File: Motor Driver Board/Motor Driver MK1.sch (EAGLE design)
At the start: 8 parts, among them X1 MAB8SH, X2 MAB8SH, X3 MAB8SH, X4 MAB8SH

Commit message: finished up schematic
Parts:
- removed U$1, U$2, U$4: DRV8825, CNC-Interface:DRV8825
- removed X2, X3, X4: MAB8SH, con-hirschmann:MAB8SH
- added AC1, XC1, YC1, ZC1: (no value), rcl:CPOL-USSANYO_SMD_F12
- added AC2, XC2, YC2, ZC2: (no value), rcl:C-USC0805
- added ADIR, AHOME, ASTP, EN, FAULT, XDIR, XHOME, XSTP, YDIR, YHOME, YSTP, ZDIR, ZHOME, ZSTP: PC817, optocoupler:PC817
- added ADIR_IN, AHOME_IN, ASTP_IN, FAULT_IN, RLED, XDIR_IN, XHOME_IN, XSTP_IN, YDIR_IN, YHOME_IN, YSTP_IN, ZDIR_IN, ZHOME_IN, ZSTP_IN: 330, resistor:R-US_R0805
- added ADIR_UP, AHOME_UP, EN_UP, FAULT_UP, XDIR_UP, XHOME_UP, YDIR_UP, YHOME_UP, ZDIR_UP, ZHOME_UP: 1k, resistor:R-US_R0805
- added ADRIVER, XDRIVER, YDRIVER: DRV8825, CNC-Interface:DRV8825
- added AFAULT, ASAMPLE, ESTOP, XFAULT, XSAMPLE, YFAULT, YSAMPLE, ZFAULT, ZSAMPLE: (no value), pinhead:PINHD-1X2
- added AHOME_OUT, FAULT_OUT, XHOME_OUT, YHOME_OUT, ZHOME_OUT: 100, resistor:R-US_R0805
- added AOUT, XOUT, YOUT, ZOUT: MAB8SH, con-hirschmann:MAB8SH
- added ASET, XSET, YSET, ZSET: (no value), pinhead:PINHD-2X3
- added ASTP_UP, EN_IN, XSTP_UP, YSTP_UP, ZSTP_UP: (no value), resistor:R-US_R0805
- added DB: PARALLEL PORT, con-thomas-betts:D-SUB25-H2R25ST
- added FAULTOUT: 4PIN, con-molex:22-23-2041
- added LED1: (no value), led:LEDCHIP-LED0805
- X1: value MAB8SH -> (none); device con-hirschmann:MAB8SH -> con-wago-500:W237-102
- renumbered U$3 to ZDRIVER
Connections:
- new net ASTP_UP: ADRIVER.STP, ASAMPLE.2, ASTP.COL, ASTP_UP.1
- new net DGND: ADIR.C, AHOME.EMIT, ASTP.C, DB-18.F, DB-19.F, DB-20.F, DB-21.F, DB-22.F, DB-23.F, DB-24.F, DB-25.F, EN.C, FAULT.EMIT, XDIR.C, XHOME.EMIT, XSTP.C, YDIR.C, YHOME.EMIT, YSTP.C, ZDIR.C, ZHOME.EMIT, ZSTP.C
- new net GND: AC1.-, AC2.2, ADIR.EMIT, ADRIVER.GND, AHOME.C, AOUT.3, AOUT.PE, ASTP.EMIT, EN.EMIT, ESTOP.2, FAULT.C, LED1.C, X1-2.KL, XC1.-, XC2.2, XDIR.EMIT, XDRIVER.GND, XHOME.C, XOUT.3, XOUT.PE, XSTP.EMIT, YC1.-, YC2.2, YDIR.EMIT, YDRIVER.GND, YHOME.C, YOUT.3, YOUT.PE, YSTP.EMIT, ZC1.-, ZC2.2, ZDIR.EMIT, ZDRIVER.GND, ZHOME.C, ZOUT.3, ZOUT.PE, ZSTP.EMIT
- new net N$15: ADRIVER.B1, AOUT.4
- new net N$16: ADRIVER.B2, AOUT.7
- new net N$17: LED1.A, RLED.1
- new net N$18: XDRIVER.STP, XSAMPLE.2, XSTP.COL, XSTP_UP.1
- new net N$19: XDRIVER.M2, XSET.2
- new net N$20: XDRIVER.M1, XSET.4
- new net N$21: XDRIVER.M0, XSET.6
- new net N$22: YDRIVER.M2, YSET.2
- new net N$23: YDRIVER.M1, YSET.4
- new net N$24: YDRIVER.M0, YSET.6
- new net N$25: ADRIVER.M2, ASET.2
- new net N$26: ADRIVER.M1, ASET.4
- new net N$27: ADRIVER.M0, ASET.6
- new net N$28: ZDRIVER.M2, ZSET.2
- new net N$29: ZDRIVER.M1, ZSET.4
- new net N$30: ZDRIVER.M0, ZSET.6
- new net N$33: ADRIVER.EN, EN.COL, EN_UP.1, ESTOP.1, XDRIVER.EN, YDRIVER.EN, ZDRIVER.EN
- new net N$35: EN.A, EN_IN.1
- new net N$37: AFAULT.2, FAULTOUT-3.S, ZDRIVER.FLT, ZFAULT.1
- new net N$38: XDIR.A, XDIR_IN.1
- new net N$39: XSTP.A, XSTP_IN.1
- new net N$40: YDIR.A, YDIR_IN.1
- new net N$41: YSTP.A, YSTP_IN.1
- new net N$42: DB-2.F, XDIR_IN.2
- new net N$43: DB-3.F, XSTP_IN.2
- new net N$44: DB-4.F, YDIR_IN.2
- new net N$45: DB-5.F, YSTP_IN.2
- new net N$46: ZSTP.A, ZSTP_IN.1
- new net N$47: ZDIR.A, ZDIR_IN.1
- new net N$48: DB-6.F, ZDIR_IN.2
- new net N$49: DB-7.F, ZSTP_IN.2
- new net N$50: ADIR.A, ADIR_IN.1
- new net N$51: ADIR_IN.2, DB-8.F
- new net N$52: ASTP_IN.2, DB-9.F
- new net N$53: ASTP.A, ASTP_IN.1
- new net N$54: DB-1.F, EN_IN.2
- new net N$55: DB-10.F, XHOME_OUT.2
- new net N$57: ADIR.COL, ADIR_UP.1, ADRIVER.DIR, ASAMPLE.1
- new net N$58: FAULT.COL, FAULT_OUT.1, FAULT_UP.1
- new net N$59: DB-15.F, FAULT_OUT.2
- new net N$60: FAULTOUT-1.S, XDRIVER.FLT, XFAULT.1, YFAULT.2
- new net N$61: FAULTOUT-2.S, YDRIVER.FLT, YFAULT.1, ZFAULT.2
- new net N$62: ADRIVER.FLT, AFAULT.1, FAULTOUT-4.S
- new net N$63: AOUT.2, FAULT.A, FAULT_IN.1, XFAULT.2, XOUT.2, YOUT.2, ZOUT.2
- new net N$64: XHOME_IN.2, XOUT.1
- new net N$65: YHOME_IN.2, YOUT.1
- new net N$66: ZHOME_IN.2, ZOUT.1
- new net N$67: AHOME_IN.2, AOUT.1
- new net N$69: YHOME.COL, YHOME_OUT.1, YHOME_UP.1
- new net N$70: XHOME.A, XHOME_IN.1
- new net N$71: YHOME.A, YHOME_IN.1
- new net N$72: ZHOME.A, ZHOME_IN.1
- new net N$73: AHOME.A, AHOME_IN.1
- new net N$74: DB-11.F, YHOME_OUT.2
- new net N$75: ZHOME.COL, ZHOME_OUT.1, ZHOME_UP.1
- new net N$76: DB-12.F, ZHOME_OUT.2
- new net N$77: AHOME_OUT.2, DB-13.F
- new net N$78: AHOME.COL, AHOME_OUT.1, AHOME_UP.1
- new net N$79: DB-14.F, FAULT_UP.2
- new net N$80: DB-17.F, XHOME_UP.2, YHOME_UP.2
- new net N$82: AHOME_UP.2, DB-16.F, ZHOME_UP.2
- new net V+: AC1.+, AC2.1, ADRIVER.VMM, RLED.2, X1-1.KL, XC1.+, XC2.1, XDRIVER.VMM, YC1.+, YC2.1, YDRIVER.VMM, ZC1.+, ZC2.1, ZDRIVER.VMM
- new net VCC: ADIR_UP.2, ADRIVER.RST, ADRIVER.SLP, AOUT.6, ASET.1, ASET.3, ASET.5, ASTP_UP.2, EN_UP.2, FAULT_IN.2, XDIR_UP.2, XDRIVER.RST, XDRIVER.SLP, XOUT.6, XSET.1, XSET.3, XSET.5, XSTP_UP.2, YDIR_UP.2, YDRIVER.RST, YDRIVER.SLP, YOUT.6, YSET.1, YSET.3, YSET.5, YSTP_UP.2, ZDIR_UP.2, ZDRIVER.RST, ZDRIVER.SLP, ZOUT.6, ZSET.1, ZSET.3, ZSET.5, ZSTP_UP.2
- new net XHOME_UP: XHOME.COL, XHOME_OUT.1, XHOME_UP.1
- new net XSAMPLE: XDIR.COL, XDIR_UP.1, XDRIVER.DIR, XSAMPLE.1
- new net YDIR: YDIR.COL, YDIR_UP.1, YDRIVER.DIR, YSAMPLE.1
- new net YSTP: YDRIVER.STP, YSAMPLE.2, YSTP.COL, YSTP_UP.1
- new net ZDIR: ZDIR.COL, ZDIR_UP.1, ZDRIVER.DIR, ZSAMPLE.1
- new net ZSTP: ZDRIVER.STP, ZSAMPLE.2, ZSTP.COL, ZSTP_UP.1
- net N$1: now also XDRIVER.A2, XOUT.8; no longer U$1.A2, X1.8
- net N$10: now also ZOUT.5; no longer X3.5
- net N$11: now also ZOUT.8; no longer X3.8
- net N$12: now also ZOUT.4; no longer X3.4
- net N$13: now also ZOUT.7; no longer X3.7
- net N$14: now also ADRIVER.A2, AOUT.8; no longer U$4.A2, X4.8
- net N$2: now also XDRIVER.A1, XOUT.5; no longer U$1.A1, X1.5
- net N$3: now also XDRIVER.B1, XOUT.4; no longer U$1.B1, X1.4
- net N$4: now also XDRIVER.B2, XOUT.7; no longer U$1.B2, X1.7
- net N$5: now also ADRIVER.A1, AOUT.5; no longer U$4.A1, X4.5
- net N$6: now also YDRIVER.A1, YOUT.5; no longer U$2.A1, X2.5
- net N$7: now also YDRIVER.A2, YOUT.8; no longer U$2.A2, X2.8
- net N$8: now also YDRIVER.B1, YOUT.4; no longer U$2.B1, X2.4
- net N$9: now also YDRIVER.B2, YOUT.7; no longer U$2.B2, X2.7

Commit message: fleshed out PCB, spent wayyy too much time today.
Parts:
- removed FAULTOUT: 4PIN, con-molex:22-23-2041
- added IC1: REG1117, burr-brown:REG1117
- added U$1: RASPBERRY-PI, RaspberryPi:RASPBERRY-PI
- AC1, XC1, YC1, ZC1: device rcl:CPOL-USSANYO_SMD_F12 -> rcl:CPOL-USSANYO_SMD_E7
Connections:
- removed net N$79: DB-14.F, FAULT_UP.2
- removed net N$80: DB-17.F, XHOME_UP.2, YHOME_UP.2
- removed net N$82: AHOME_UP.2, DB-16.F, ZHOME_UP.2
- net GND: now also IC1.GND
- net N$37: no longer FAULTOUT-3.S
- net N$42: now also ADIR_IN.2, DB-9.F; no longer DB-2.F, XDIR_IN.2
- net N$43: now also ASTP_IN.2, DB-8.F; no longer DB-3.F, XSTP_IN.2
- net N$44: now also DB-7.F, ZDIR_IN.2; no longer DB-4.F, YDIR_IN.2
- net N$45: now also DB-6.F, ZSTP_IN.2; no longer DB-5.F, YSTP_IN.2
- net N$48: now also DB-5.F, YDIR_IN.2; no longer DB-6.F, ZDIR_IN.2
- net N$49: now also DB-4.F, YSTP_IN.2; no longer DB-7.F, ZSTP_IN.2
- net N$51: now also DB-3.F, XDIR_IN.2; no longer ADIR_IN.2, DB-8.F
- net N$52: now also DB-2.F, XSTP_IN.2; no longer ASTP_IN.2, DB-9.F
- net N$60: no longer FAULTOUT-1.S
- net N$61: no longer FAULTOUT-2.S
- net N$62: no longer FAULTOUT-4.S
- net V+: now also IC1.VIN
- net VCC: now also AHOME_UP.2, FAULT_UP.2, IC1.VOUT, XHOME_UP.2, YHOME_UP.2, ZHOME_UP.2
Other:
- moved on the sheet: DB-14, DB-16, DB-17, DB-2, DB-3, DB-4, DB-5, DB-6, DB-7, DB-8, DB-9

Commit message: Day 2. Everything is lines. How much further can this go?
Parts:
- added AC3: (no value), rcl:C-USC0805
- added LED2: (no value), led:LEDCHIP-LED0805
- added RLED1: 330, resistor:R-US_R0805
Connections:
- new net N$31: LED2.A, RLED1.2
- net GND: now also AC3.2, LED2.C
- net VCC: now also AC3.1, RLED1.1
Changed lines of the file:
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@@
 <part name="P+23" library="supply1" deviceset="VCC" device=""/>
 <part name="P+24" library="supply1" deviceset="VCC" device=""/>
+<part name="AC3" library="rcl" deviceset="C-US" device="C0805"/>
+<part name="RLED1" library="resistor" deviceset="R-US_" device="R0805" value="330"/>
+<part name="LED2" library="led" deviceset="LED" device="CHIP-LED0805"/>
 </parts>
 <sheets>
@@
 <instance part="IC1" gate="G$1" x="220.98" y="137.16"/>
 <instance part="SUPPLY49" gate="1" x="205.74" y="137.16" rot="R90"/>
-<instance part="SUPPLY50" gate="GND" x="220.98" y="121.92"/>
-<instance part="P+19" gate="VCC" x="236.22" y="137.16" smashed="yes" rot="R270">
-<attribute name="VALUE" x="238.76" y="137.16" size="1.778" layer="96"/>
+<instance part="SUPPLY50" gate="GND" x="220.98" y="116.84"/>
+<instance part="P+19" gate="VCC" x="236.22" y="142.24" smashed="yes">
+<attribute name="VALUE" x="236.22" y="144.78" size="1.778" layer="96" rot="R90"/>
 </instance>
 <instance part="P+20" gate="VCC" x="165.1" y="152.4" smashed="yes">
@@
 <attribute name="VALUE" x="165.1" y="-22.86" size="1.778" layer="96" rot="R90"/>
 </instance>
+<instance part="AC3" gate="G$1" x="236.22" y="132.08"/>
+<instance part="RLED1" gate="G$1" x="243.84" y="137.16"/>
+<instance part="LED2" gate="G$1" x="251.46" y="132.08"/>
 </instances>
 <busses>
@@
 <pinref part="IC1" gate="G$1" pin="GND"/>
 <pinref part="SUPPLY50" gate="GND" pin="GND"/>
+<wire x1="220.98" y1="119.38" x2="220.98" y2="124.46" width="0.1524" layer="91"/>
+<pinref part="LED2" gate="G$1" pin="C"/>
+<wire x1="251.46" y1="127" x2="251.46" y2="124.46" width="0.1524" layer="91"/>
+<pinref part="AC3" gate="G$1" pin="2"/>
+<wire x1="251.46" y1="124.46" x2="236.22" y2="124.46" width="0.1524" layer="91"/>
+<wire x1="236.22" y1="127" x2="236.22" y2="124.46" width="0.1524" layer="91"/>
+<wire x1="236.22" y1="124.46" x2="220.98" y2="124.46" width="0.1524" layer="91"/>
 </segment>
 </net>
@@
 <pinref part="IC1" gate="G$1" pin="VOUT"/>
 <pinref part="P+19" gate="VCC" pin="VCC"/>
+<wire x1="236.22" y1="139.7" x2="236.22" y2="137.16" width="0.1524" layer="91"/>
+<pinref part="AC3" gate="G$1" pin="1"/>
+<wire x1="236.22" y1="137.16" x2="233.68" y2="137.16" width="0.1524" layer="91"/>
+<wire x1="236.22" y1="134.62" x2="236.22" y2="137.16" width="0.1524" layer="91"/>
+<pinref part="RLED1" gate="G$1" pin="1"/>
+<wire x1="236.22" y1="137.16" x2="238.76" y2="137.16" width="0.1524" layer="91"/>
 </segment>
 <segment>
@@
 </segment>
 </net>
+<net name="N$31" class="0">
+<segment>
+<pinref part="RLED1" gate="G$1" pin="2"/>
+<pinref part="LED2" gate="G$1" pin="A"/>
+<wire x1="248.92" y1="137.16" x2="251.46" y2="137.16" width="0.1524" layer="91"/>
+<wire x1="251.46" y1="137.16" x2="251.46" y2="134.62" width="0.1524" layer="91"/>
+</segment>
+</net>

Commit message: MKII is almost complete, cleaned a lot of stuff up.
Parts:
- removed AFAULT, ASAMPLE, ESTOP, XFAULT, XSAMPLE, YFAULT, YSAMPLE, ZFAULT, ZSAMPLE: (no value), pinhead:PINHD-1X2
- added AC4, AC5, AC6, AC7: (no value), rcl:C-USC0805
- added JP1, JP10, JP11, JP12, JP13, JP14, JP15, JP16, JP17, JP18, JP2, JP3, JP4, JP5, JP6, JP7, JP8, JP9: (no value), pinhead:PINHD-1X1
- renumbered AHOME to AHOM, XHOME to XHOM, YHOME to YHOM, ZHOME to ZHOM
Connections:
- removed net N$33: ADRIVER.EN, EN.COL, EN_UP.1, ESTOP.1, XDRIVER.EN, YDRIVER.EN, ZDRIVER.EN
- removed net N$48: DB-5.F, YDIR_IN.2
- new net N$36: ADRIVER.EN, EN.COL, EN_UP.1, JP1.1, XDRIVER.EN, YDRIVER.EN, ZDRIVER.EN
- new net N$84: DB-7.F, ZSTP_IN.2
- net ASTP_UP: now also JP10.1; no longer ASAMPLE.2
- net GND: now also AC4.2, AC5.2, AC6.2, AC7.2, JP2.1; no longer ESTOP.2
- net N$18: now also JP4.1; no longer XSAMPLE.2
- net N$19: now also XSET.1; no longer XSET.2
- net N$20: now also XSET.3; no longer XSET.4
- net N$21: now also XSET.5; no longer XSET.6
- net N$22: now also YSET.1; no longer YSET.2
- net N$23: now also YSET.3; no longer YSET.4
- net N$24: now also YSET.5; no longer YSET.6
- net N$25: now also ASET.1; no longer ASET.2
- net N$26: now also ASET.3; no longer ASET.4
- net N$27: now also ASET.5; no longer ASET.6
- net N$28: now also ZSET.1; no longer ZSET.2
- net N$29: now also ZSET.3; no longer ZSET.4
- net N$30: now also ZSET.5; no longer ZSET.6
- net N$37: now also JP11.1, JP14.1; no longer AFAULT.2, ZFAULT.1
- net N$42: now also DB-3.F, XSTP_IN.2; no longer ADIR_IN.2, DB-9.F
- net N$43: now also DB-2.F, XDIR_IN.2; no longer ASTP_IN.2, DB-8.F
- net N$44: now also DB-5.F, YSTP_IN.2; no longer DB-7.F, ZDIR_IN.2
- net N$45: now also DB-4.F, YDIR_IN.2; no longer DB-6.F, ZSTP_IN.2
- net N$49: now also DB-6.F, ZDIR_IN.2; no longer DB-4.F, YSTP_IN.2
- net N$51: now also ASTP_IN.2, DB-9.F; no longer DB-3.F, XDIR_IN.2
- net N$52: now also ADIR_IN.2, DB-8.F; no longer DB-2.F, XSTP_IN.2
- net N$56: now also JP17.1; no longer XFAULT.2
- net N$57: now also JP9.1; no longer ASAMPLE.1
- net N$60: now also JP15.1, JP18.1; no longer XFAULT.1, YFAULT.2
- net N$61: now also JP13.1, JP16.1; no longer YFAULT.1, ZFAULT.2
- net N$62: now also JP12.1; no longer AFAULT.1
- net VCC: now also AC4.1, AC5.1, AC6.1, AC7.1, ASET.2, ASET.4, ASET.6, XSET.2, XSET.4, XSET.6, YSET.2, YSET.4, YSET.6, ZSET.2, ZSET.4, ZSET.6; no longer ASET.1, ASET.3, ASET.5, XSET.1, XSET.3, XSET.5, YSET.1, YSET.3, YSET.5, ZSET.1, ZSET.3, ZSET.5
- net XSAMPLE: now also JP3.1; no longer XSAMPLE.1
- net YDIR: now also JP5.1; no longer YSAMPLE.1
- net YSTP: now also JP6.1; no longer YSAMPLE.2
- net ZDIR: now also JP7.1; no longer ZSAMPLE.1
- net ZSTP: now also JP8.1; no longer ZSAMPLE.2
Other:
- moved on the sheet: DB-2, DB-3, DB-4, DB-5, DB-6, DB-7, DB-8, DB-9

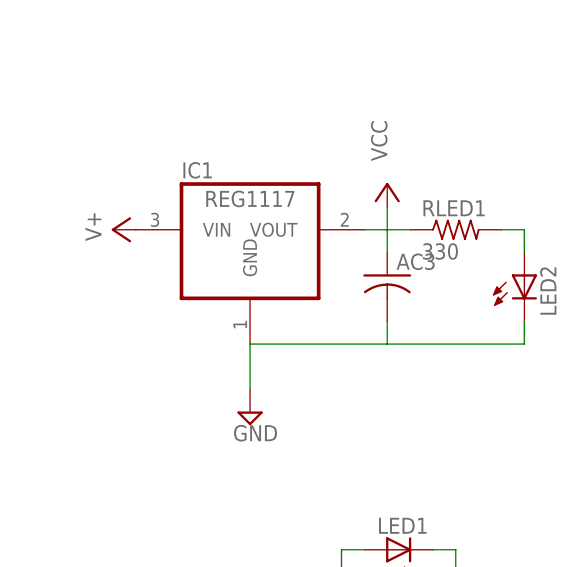
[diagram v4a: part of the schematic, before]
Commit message: Finished up control board. Pending second review.
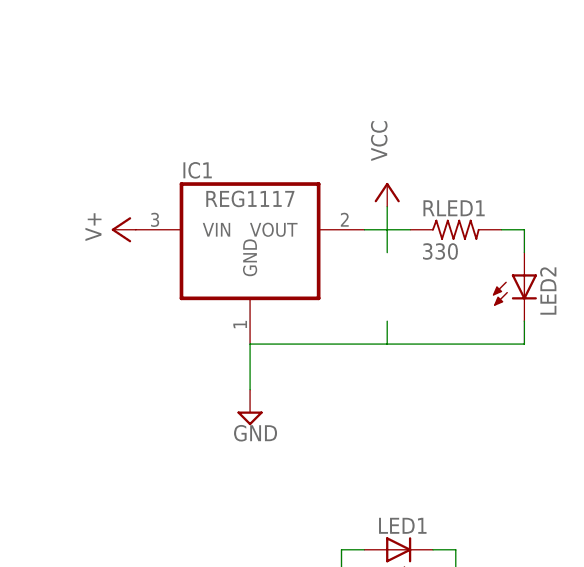
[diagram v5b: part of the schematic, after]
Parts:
- removed AC3: (no value), rcl:C-USC0805
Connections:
- net XHOME_UP renamed N$64
- net GND: no longer AC3.2
- net VCC: no longer AC3.1
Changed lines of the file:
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@@
 <part name="P+23" library="supply1" deviceset="VCC" device=""/>
 <part name="P+24" library="supply1" deviceset="VCC" device=""/>
-<part name="AC3" library="rcl" deviceset="C-US" device="C0805"/>
 <part name="RLED1" library="resistor" deviceset="R-US_" device="R0805" value="330"/>
 <part name="LED2" library="led" deviceset="LED" device="CHIP-LED0805"/>
@@
 <attribute name="VALUE" x="165.1" y="-22.86" size="1.778" layer="96" rot="R90"/>
 </instance>
-<instance part="AC3" gate="G$1" x="236.22" y="132.08"/>
 <instance part="RLED1" gate="G$1" x="243.84" y="137.16"/>
 <instance part="LED2" gate="G$1" x="251.46" y="132.08"/>
@@
 <pinref part="LED2" gate="G$1" pin="C"/>
 <wire x1="251.46" y1="127" x2="251.46" y2="124.46" width="0.1524" layer="91"/>
-<pinref part="AC3" gate="G$1" pin="2"/>
 <wire x1="251.46" y1="124.46" x2="236.22" y2="124.46" width="0.1524" layer="91"/>
 <wire x1="236.22" y1="127" x2="236.22" y2="124.46" width="0.1524" layer="91"/>
@@
 </segment>
 </net>
-<net name="XHOME_UP" class="0">
+<net name="N$64" class="0">
 <segment>
 <pinref part="XHOM" gate="A" pin="COL"/>
@@
 </segment>
 </net>
-<net name="N$69" class="0">
+<net name="N$87" class="0">
 <segment>
 <pinref part="YHOM" gate="A" pin="COL"/>
@@
 </segment>
 </net>
-<net name="N$75" class="0">
+<net name="N$89" class="0">
 <segment>
 <pinref part="ZHOM" gate="A" pin="COL"/>
@@
 </segment>
 </net>
-<net name="N$78" class="0">
+<net name="N$48" class="0">
 <segment>
 <pinref part="AHOM" gate="A" pin="COL"/>
@@
 </segment>
 </net>
-<net name="N$17" class="0">
+<net name="N$76" class="0">
 <segment>
 <pinref part="LED1" gate="G$1" pin="A"/>
@@
 <pinref part="P+19" gate="VCC" pin="VCC"/>
 <wire x1="236.22" y1="139.7" x2="236.22" y2="137.16" width="0.1524" layer="91"/>
-<pinref part="AC3" gate="G$1" pin="1"/>
 <wire x1="236.22" y1="137.16" x2="233.68" y2="137.16" width="0.1524" layer="91"/>
 <wire x1="236.22" y1="134.62" x2="236.22" y2="137.16" width="0.1524" layer="91"/>

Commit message: 8+ hours since last remote commit. Going to let it sit for now.
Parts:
- removed U$1: RASPBERRY-PI, RaspberryPi:RASPBERRY-PI
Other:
- moved on the sheet: IC1, LED2, RLED1
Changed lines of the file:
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@@
 <part name="RLED" library="resistor" deviceset="R-US_" device="R0805" value="330"/>
 <part name="FRAME1" library="frames" deviceset="FRAME_B_L" device=""/>
-<part name="U$1" library="RaspberryPi" deviceset="RASPBERRY-PI" device=""/>
 <part name="IC1" library="burr-brown" deviceset="REG1117" device=""/>
 <part name="SUPPLY49" library="supply2" deviceset="V+" device=""/>
@@
 <instance part="FRAME1" gate="G$1" x="-147.32" y="-93.98"/>
 <instance part="FRAME1" gate="G$2" x="177.8" y="-93.98"/>
-<instance part="U$1" gate="G$1" x="-109.22" y="111.76"/>
-<instance part="IC1" gate="G$1" x="220.98" y="137.16"/>
-<instance part="SUPPLY49" gate="1" x="205.74" y="137.16" rot="R90"/>
-<instance part="SUPPLY50" gate="GND" x="220.98" y="116.84"/>
-<instance part="P+19" gate="VCC" x="236.22" y="142.24" smashed="yes">
-<attribute name="VALUE" x="236.22" y="144.78" size="1.778" layer="96" rot="R90"/>
+<instance part="IC1" gate="G$1" x="231.14" y="127" rot="R90"/>
+<instance part="SUPPLY49" gate="1" x="226.06" y="111.76" rot="R90"/>
+<instance part="SUPPLY50" gate="GND" x="251.46" y="127" rot="R90"/>
+<instance part="P+19" gate="VCC" x="226.06" y="142.24" smashed="yes" rot="R90">
+<attribute name="VALUE" x="223.52" y="142.24" size="1.778" layer="96" rot="R180"/>
 </instance>
 <instance part="P+20" gate="VCC" x="165.1" y="152.4" smashed="yes">
@@
 <attribute name="VALUE" x="165.1" y="-22.86" size="1.778" layer="96" rot="R90"/>
 </instance>
-<instance part="RLED1" gate="G$1" x="243.84" y="137.16"/>
-<instance part="LED2" gate="G$1" x="251.46" y="132.08"/>
+<instance part="RLED1" gate="G$1" x="231.14" y="149.86" rot="R90"/>
+<instance part="LED2" gate="G$1" x="236.22" y="157.48" rot="R90"/>
 <instance part="JP1" gate="G$1" x="20.32" y="144.78" rot="R90"/>
 <instance part="JP2" gate="G$1" x="25.4" y="144.78" rot="R90"/>
@@
 <pinref part="IC1" gate="G$1" pin="VIN"/>
 <pinref part="SUPPLY49" gate="1" pin="V+"/>
+<wire x1="228.6" y1="111.76" x2="231.14" y2="111.76" width="0.1524" layer="91"/>
+<wire x1="231.14" y1="111.76" x2="231.14" y2="114.3" width="0.1524" layer="91"/>
 </segment>
 </net>
@@
 <pinref part="IC1" gate="G$1" pin="GND"/>
 <pinref part="SUPPLY50" gate="GND" pin="GND"/>
-<wire x1="220.98" y1="119.38" x2="220.98" y2="124.46" width="0.1524" layer="91"/>
+<wire x1="248.92" y1="127" x2="243.84" y2="127" width="0.1524" layer="91"/>
 <pinref part="LED2" gate="G$1" pin="C"/>
-<wire x1="251.46" y1="127" x2="251.46" y2="124.46" width="0.1524" layer="91"/>
-<wire x1="251.46" y1="124.46" x2="236.22" y2="124.46" width="0.1524" layer="91"/>
-<wire x1="236.22" y1="127" x2="236.22" y2="124.46" width="0.1524" layer="91"/>
-<wire x1="236.22" y1="124.46" x2="220.98" y2="124.46" width="0.1524" layer="91"/>
+<wire x1="241.3" y1="157.48" x2="243.84" y2="157.48" width="0.1524" layer="91"/>
+<wire x1="243.84" y1="157.48" x2="243.84" y2="127" width="0.1524" layer="91"/>
 </segment>
 <segment>
@@
 <pinref part="IC1" gate="G$1" pin="VOUT"/>
 <pinref part="P+19" gate="VCC" pin="VCC"/>
-<wire x1="236.22" y1="139.7" x2="236.22" y2="137.16" width="0.1524" layer="91"/>
-<wire x1="236.22" y1="137.16" x2="233.68" y2="137.16" width="0.1524" layer="91"/>
-<wire x1="236.22" y1="134.62" x2="236.22" y2="137.16" width="0.1524" layer="91"/>
+<wire x1="228.6" y1="142.24" x2="231.14" y2="142.24" width="0.1524" layer="91"/>
+<wire x1="231.14" y1="142.24" x2="231.14" y2="139.7" width="0.1524" layer="91"/>
 <pinref part="RLED1" gate="G$1" pin="1"/>
-<wire x1="236.22" y1="137.16" x2="238.76" y2="137.16" width="0.1524" layer="91"/>
+<wire x1="231.14" y1="142.24" x2="231.14" y2="144.78" width="0.1524" layer="91"/>
 </segment>
 <segment>
@@
 <pinref part="ASET" gate="A" pin="4"/>
 <wire x1="7.62" y1="-45.72" x2="15.24" y2="-45.72" width="0.1524" layer="91"/>
-<wire x1="15.24" y1="-45.72" x2="15.24" y2="-48.26" width="0.1524" layer="91"/>
 <wire x1="15.24" y1="-48.26" x2="7.62" y2="-48.26" width="0.1524" layer="91"/>
 <pinref part="ASET" gate="A" pin="6"/>
@@
 <pinref part="RLED1" gate="G$1" pin="2"/>
 <pinref part="LED2" gate="G$1" pin="A"/>
-<wire x1="248.92" y1="137.16" x2="251.46" y2="137.16" width="0.1524" layer="91"/>
-<wire x1="251.46" y1="137.16" x2="251.46" y2="134.62" width="0.1524" layer="91"/>
-</segment>
-</net>
+<wire x1="231.14" y1="154.94" x2="231.14" y2="157.48" width="0.1524" layer="91"/>
+<wire x1="231.14" y1="157.48" x2="233.68" y2="157.48" width="0.1524" layer="91"/>
+</segment>
+</net>

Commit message: added comments, more cleanup.
Signed-off-by: Evan Milton <evan@bp2e.net>
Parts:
- AC1, XC1, YC1, ZC1: value (none) -> 100uF
- AC2, AC3, XC2, XC3, YC2, YC3, ZC2, ZC3: value (none) -> 100nF
- AHOME_OUT, FAULT_OUT, XHOME_OUT, YHOME_OUT, ZHOME_OUT: value 100 -> 1k
- AHOME_UP, FAULT_UP, XHOME_UP, YHOME_UP, ZHOME_UP: value 1k -> 100k
- EN_IN: value (none) -> 330
- renumbered AC4 to XC3, AC5 to YC3, AC6 to ZC3, AC7 to AC3
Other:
- note added: "* Needs testing! Omitted second power supply on output, higher value pullup resistors should be sufficient."
- note added: "Opted for lower value pullup resistor on input to improve response time. See PC817 datasheet."
- moved on the sheet: DB-14, DB-16, DB-17
